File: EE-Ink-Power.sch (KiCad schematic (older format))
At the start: 70 parts

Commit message: Moved some little things around and created netlist.
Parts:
- gave numbers to parts that had none: 70

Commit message: Minor changes.
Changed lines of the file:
@@
 	8550 5700 8550 5200
-Wire Wire Line
-	8550 5200 9400 5200
-Wire Wire Line
-	9400 5050 9400 5250
-Connection ~ 9400 5200
 Wire Wire Line
 	9000 5300 9000 5200
@@
 $EndComp
 Wire Wire Line
-	9200 5100 9200 5200
+	9200 5200 9200 5100
 Connection ~ 9200 5200
 $Comp
@@
 Wire Wire Line
 	1650 1500 2550 1500
+Wire Wire Line
+	9400 5250 9400 5050
+Wire Wire Line
+	8550 5200 9400 5200
+Connection ~ 9400 5200
 $EndSCHEMATC

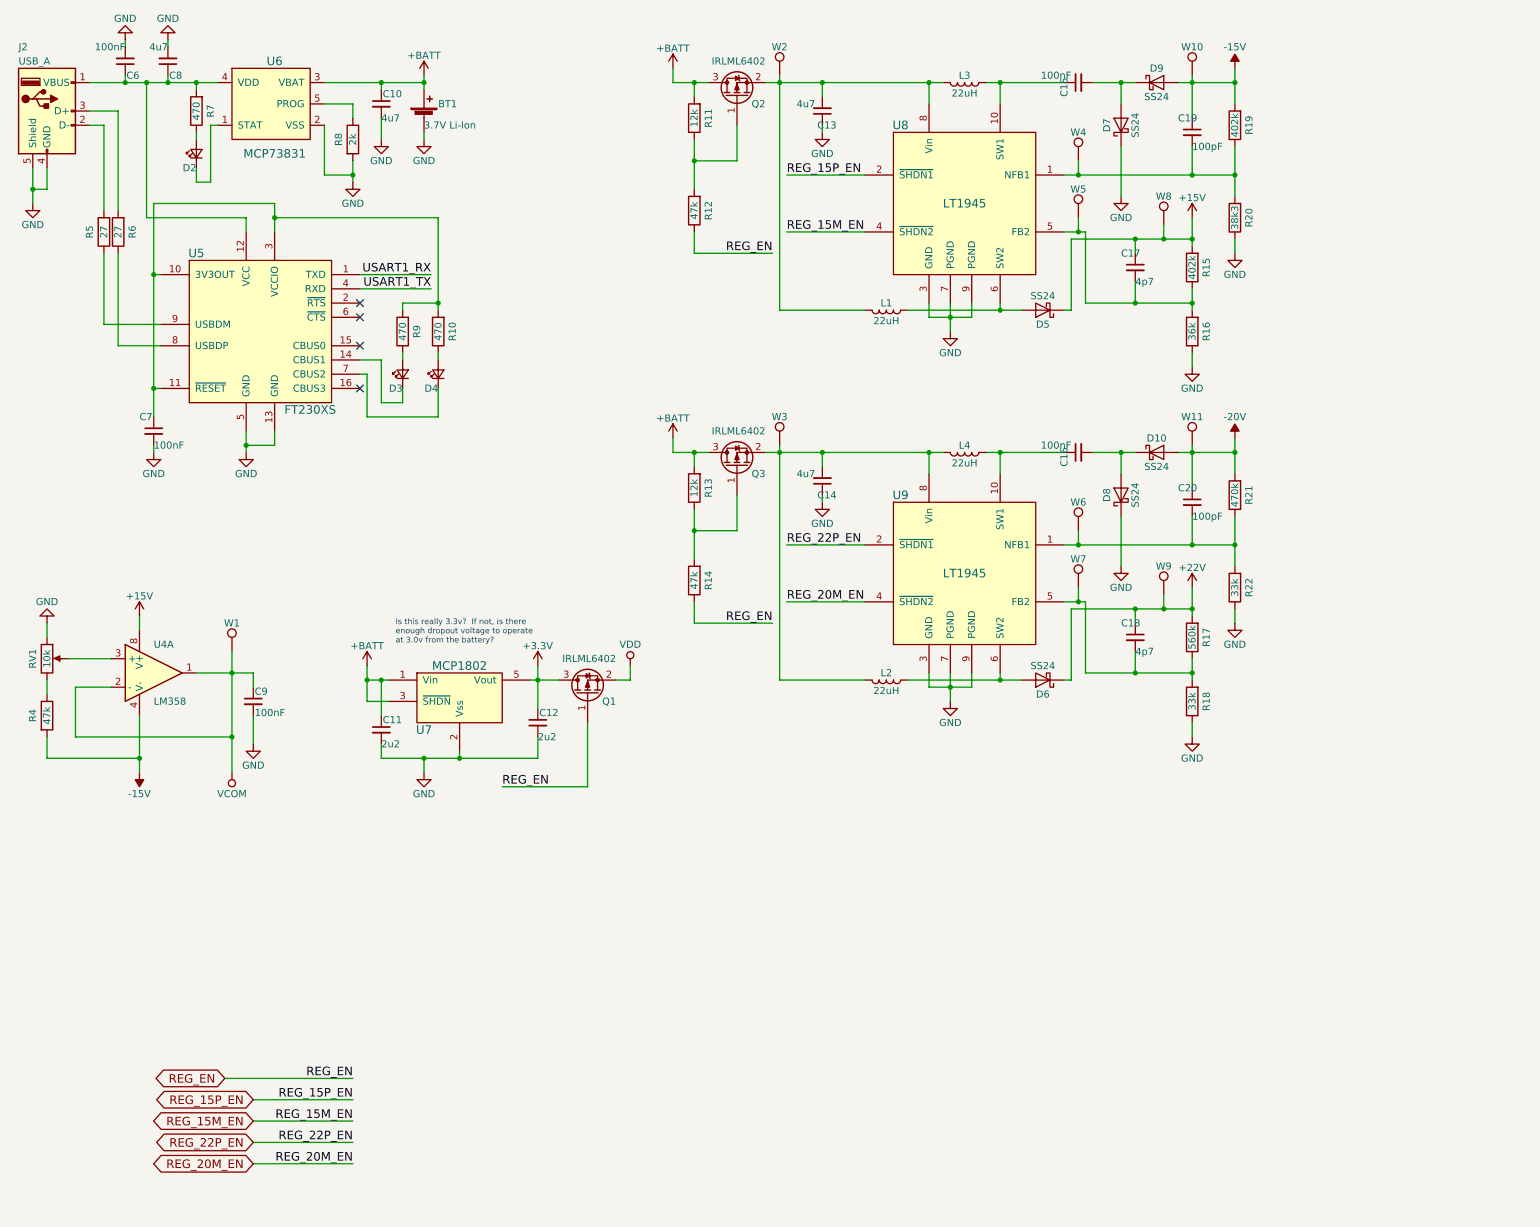
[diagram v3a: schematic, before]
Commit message: Re-arranged components (namely the FTDI chip) and created new power symbols for 3v and VBUS.
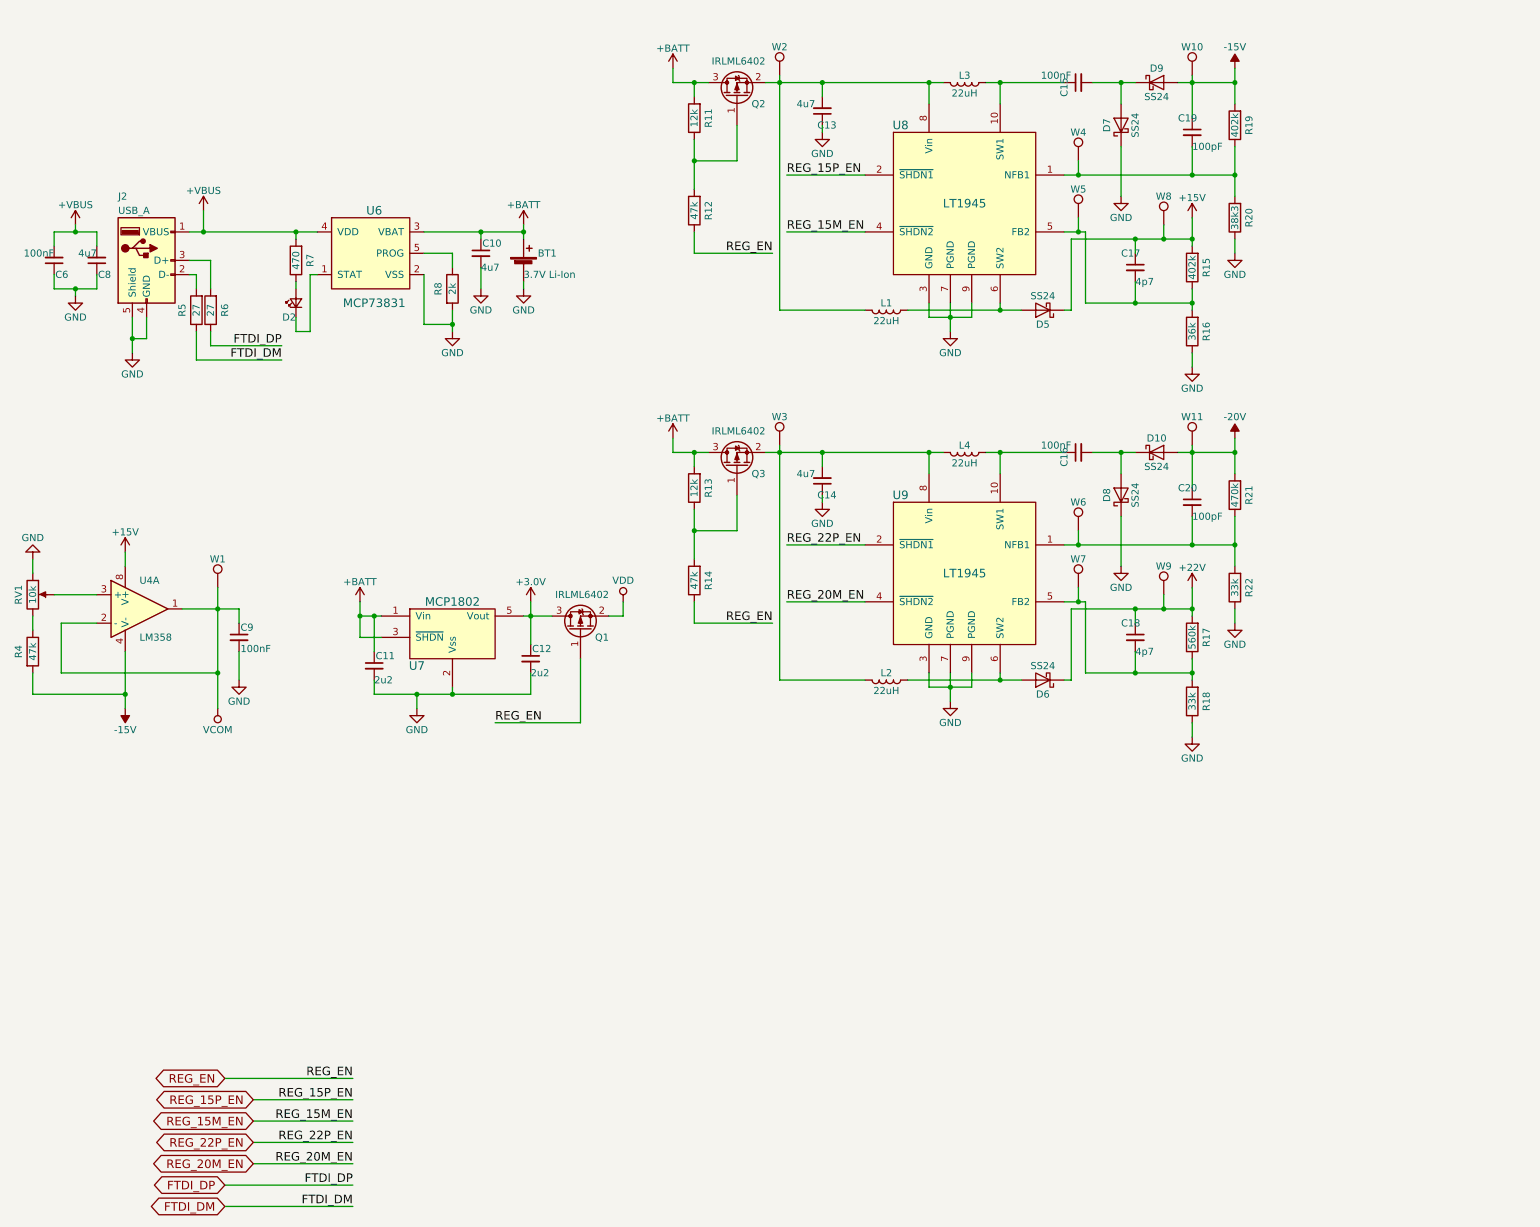
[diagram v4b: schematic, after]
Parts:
- removed C7: 100nF, symbol C_Small
- removed D3, D4: LED_Small, symbol LED_Small
- removed R10, R9: 470, symbol R
- removed U5: FT230XS, symbol FT230XS
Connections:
- net GND: now also C6.1, C8.1; no longer C6.2, C8.2
- net +VBUS: now reaches J2.1 (VBUS), R7.2, U6.4 (VDD)
- net +VBUS: now also C6.2, C8.2; no longer C6.1, C8.1
- net FTDI_DP: now reaches R6.1
- net FTDI_DM: now reaches R5.1
- net +3V3 renamed +3.0V
- no-connect marks 4 -> 0
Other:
- note removed: "Is this really 3.3v? If not, is there \nenough dropout voltage to operate \nat 3.0v from the battery?"
- moved on the sheet: BT1, C10, C11, C12, C6, C8, C9, D2, J2, Q1, R4, R5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

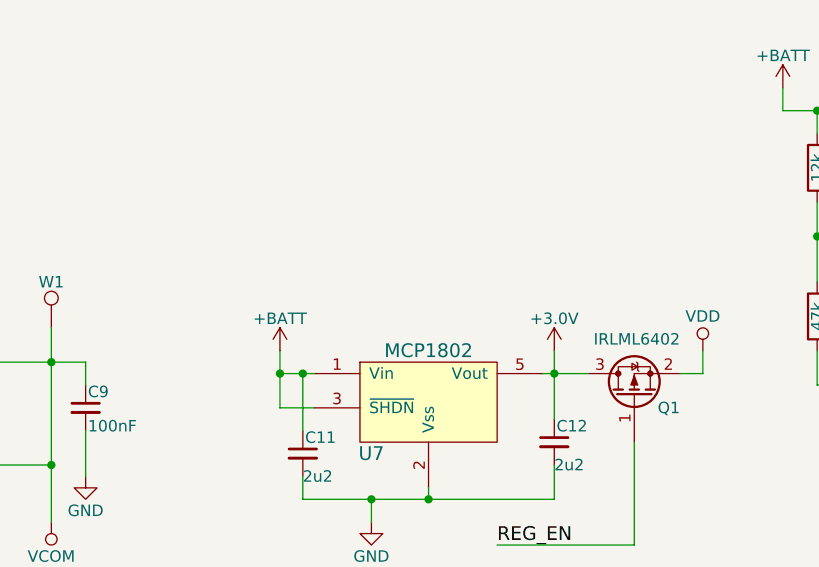
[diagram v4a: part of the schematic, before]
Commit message: Updated regulator.
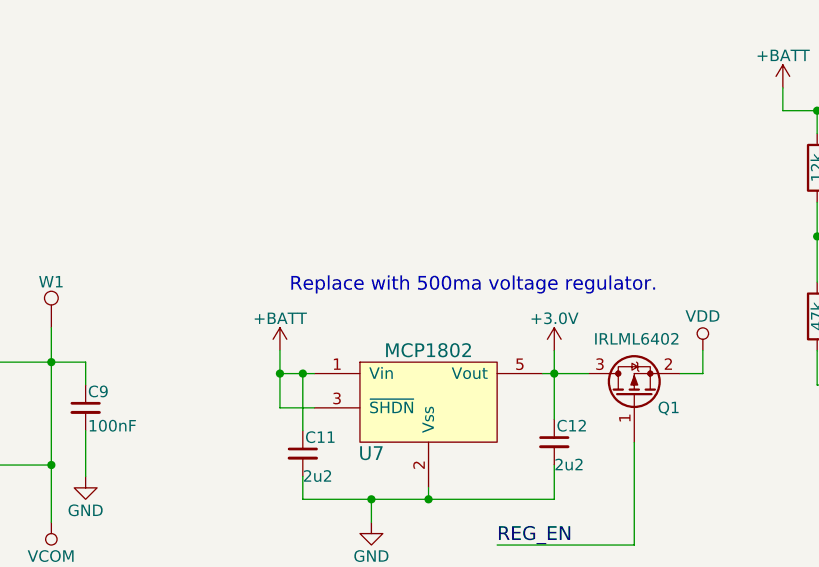
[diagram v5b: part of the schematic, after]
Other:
- note added: "Replace with 500ma voltage regulator."
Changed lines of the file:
@@
 Text GLabel 2600 9250 0    60   BiDi ~ 0
 FTDI_DP
+Text Notes 5200 4900 2    60   ~ 0
+Replace with 500ma voltage regulator.
 $EndSCHEMATC

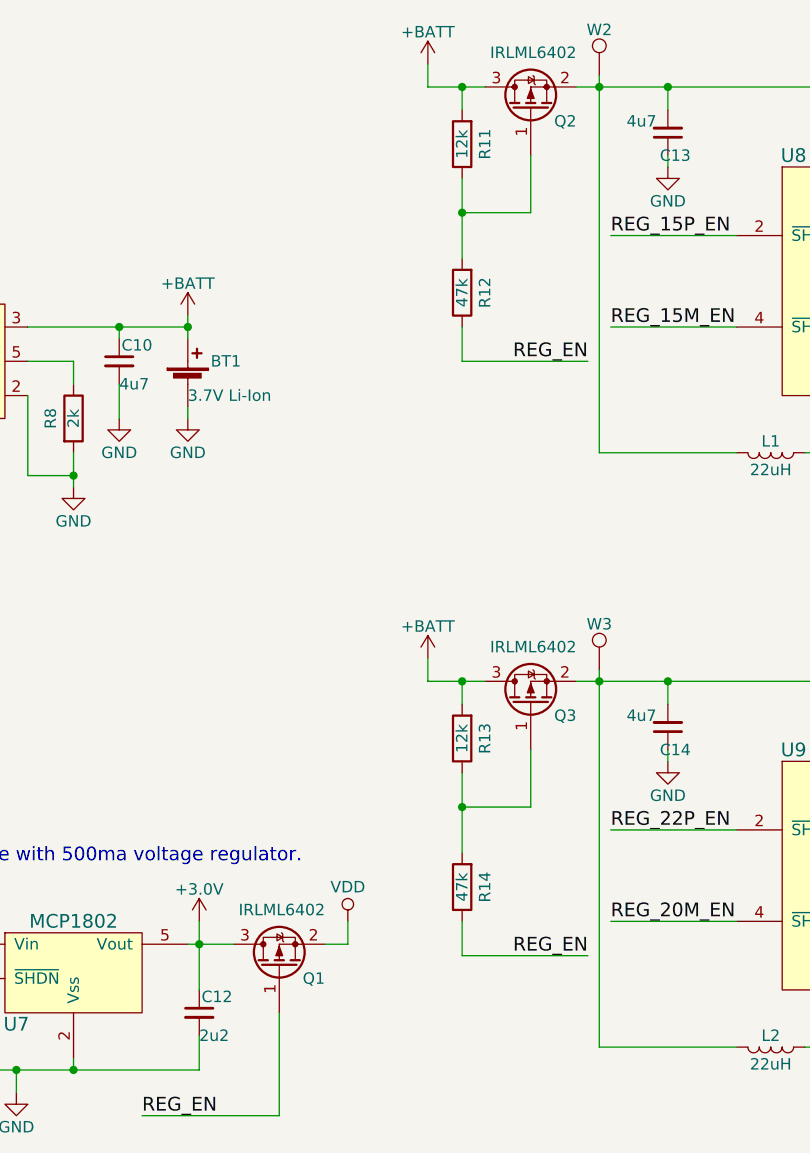
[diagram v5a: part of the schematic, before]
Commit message: Fixing transistor connections and adding UART stuff.
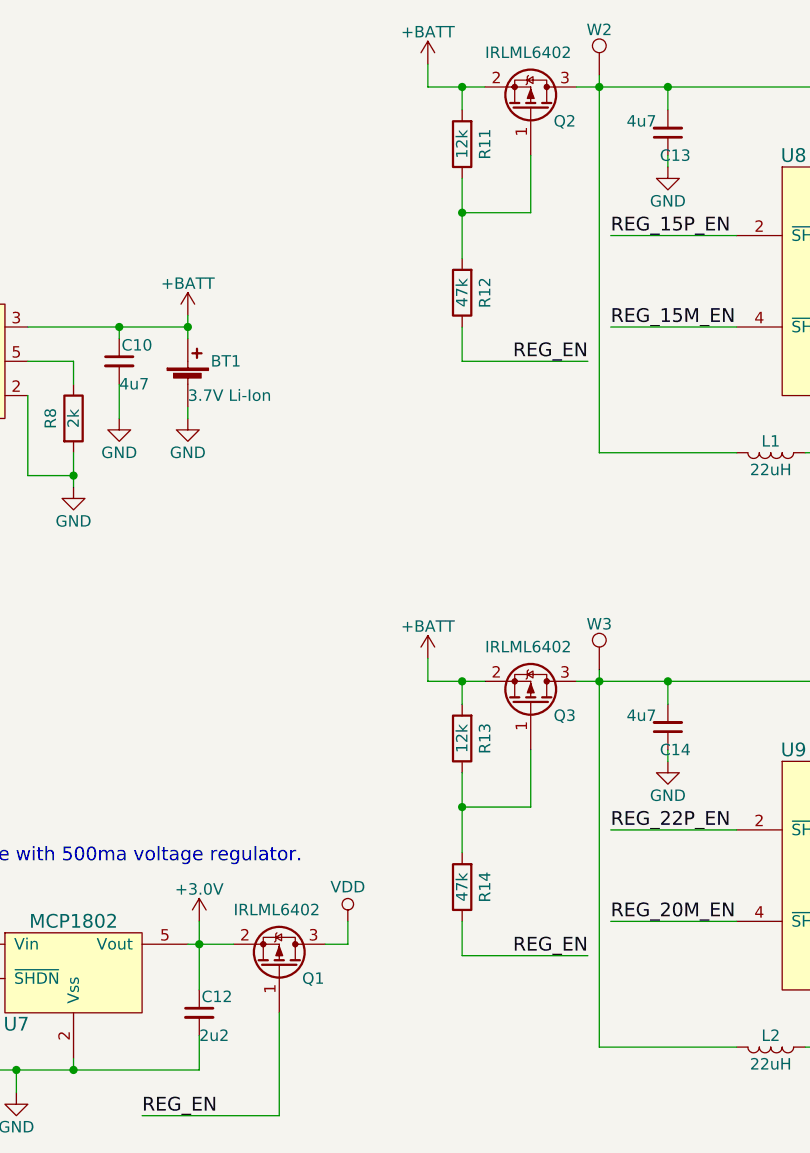
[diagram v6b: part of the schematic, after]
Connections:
- net +3.0V: now also Q1.2 (S); no longer Q1.3 (D)
- net +BATT: now also Q2.2 (S), Q3.2 (S); no longer Q2.3 (D), Q3.3 (D)
- net VDD: now also Q1.3 (D); no longer Q1.2 (S)
- net at C13.2, L1.2, L3.2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: now also Q2.3 (D); no longer Q2.2 (S)
- net at C14.2, L2.2, L4.2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: now also Q3.3 (D); no longer Q3.2 (S)
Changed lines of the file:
@@
 U 1 1 58F29C92
 P 6200 1600
-F 0 "Q2" V 6150 1400 50  0000 L CNN
+F 0 "Q2" V 6150 1700 50  0000 L CNN
 F 1 "IRLML6402" V 6450 1400 50  0000 L CNN
 F 2 "" H 6400 1700 50  0001 C CNN
 F 3 "" H 6200 1600 50  0001 C CNN
 	1    6200 1600
-	0    -1   -1   0
+	0    1    -1   0
 $EndComp
 $Comp
@@
 U 1 1 58F29D6E
 P 6200 4200
-F 0 "Q3" V 6150 4000 50  0000 L CNN
+F 0 "Q3" V 6150 4300 50  0000 L CNN
 F 1 "IRLML6402" V 6450 4000 50  0000 L CNN
 F 2 "" H 6400 4300 50  0001 C CNN
 F 3 "" H 6200 4200 50  0001 C CNN
 	1    6200 4200
-	0    -1   -1   0
+	0    1    -1   0
 $EndComp
 $Comp
@@
 U 1 1 58F2D149
 P 5100 5350
-F 0 "Q1" V 5050 5150 50  0000 L CNN
+F 0 "Q1" V 5050 5450 50  0000 L CNN
 F 1 "IRLML6402" V 5350 5150 50  0000 L CNN
 F 2 "" H 5300 5450 50  0001 C CNN
 F 3 "" H 5100 5350 50  0001 C CNN
 	1    5100 5350
-	0    -1   -1   0
-$EndComp
-$Comp
+	0    1    -1   0
+$EndComp
+$Comp
